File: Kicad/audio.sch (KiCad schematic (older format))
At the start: 70 parts, among them J601 CD Audio In, J602 AC'97 Audio Header, J603 Line Out, U601 TLV320AIC23BPW, U602 STX-4335-5BGP-S1, Y601 12M

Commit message: Fix spaces in MPNs.
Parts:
- FB601, FB602, FB603, FB605, FB606, FB607, FB609, FB610, FB611: MPN BLM21PG221SN1D -> BLM21PG221SN1D
- R606, R607, R611, R612: MPN RMCF0805FT47K5 -> RMCF0805FT47K5
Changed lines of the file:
@@
 F 4 "0" H 4850 1650 50  0001 C CNN "DNP"
 F 5 "RMCF0805FT47K5-ND" H 4850 1650 50  0001 C CNN "Digikey"
-F 6 "RMCF0805FT47K5 " H 4850 1650 50  0001 C CNN "MPN"
+F 6 "RMCF0805FT47K5" H 4850 1650 50  0001 C CNN "MPN"
 F 7 "Stackpole" H 4850 1650 50  0001 C CNN "Manufacturer"
 	1    4850 1650
@@
 F 4 "0" H 5250 1650 50  0001 C CNN "DNP"
 F 5 "RMCF0805FT47K5-ND" H 5250 1650 50  0001 C CNN "Digikey"
-F 6 "RMCF0805FT47K5 " H 5250 1650 50  0001 C CNN "MPN"
+F 6 "RMCF0805FT47K5" H 5250 1650 50  0001 C CNN "MPN"
 F 7 "Stackpole" H 5250 1650 50  0001 C CNN "Manufacturer"
 	1    5250 1650
@@
 F 2 "Inductor_SMD:L_0805_2012Metric_Pad1.15x1.40mm_HandSolder" V 6680 1400 50  0001 C CNN
 F 3 "https://www.murata.com/en-us/products/en-us/products/productdata/8796738977822/ENFA0005.pdf" H 6750 1400 50  0001 C CNN
-F 4 "BLM21PG221SN1D " H 6750 1400 50  0001 C CNN "MPN"
+F 4 "BLM21PG221SN1D" H 6750 1400 50  0001 C CNN "MPN"
 F 5 "0" H 6750 1400 50  0001 C CNN "DNP"
 F 6 "490-1054-1-ND" H 6750 1400 50  0001 C CNN "Digikey"
@@
 F 4 "0" H 4850 2850 50  0001 C CNN "DNP"
 F 5 "RMCF0805FT47K5-ND" H 4850 2850 50  0001 C CNN "Digikey"
-F 6 "RMCF0805FT47K5 " H 4850 2850 50  0001 C CNN "MPN"
+F 6 "RMCF0805FT47K5" H 4850 2850 50  0001 C CNN "MPN"
 F 7 "Stackpole" H 4850 2850 50  0001 C CNN "Manufacturer"
 	1    4850 2850
@@
 F 4 "0" H 5250 2850 50  0001 C CNN "DNP"
 F 5 "RMCF0805FT47K5-ND" H 5250 2850 50  0001 C CNN "Digikey"
-F 6 "RMCF0805FT47K5 " H 5250 2850 50  0001 C CNN "MPN"
+F 6 "RMCF0805FT47K5" H 5250 2850 50  0001 C CNN "MPN"
 F 7 "Stackpole" H 5250 2850 50  0001 C CNN "Manufacturer"
 	1    5250 2850
@@
 F 2 "Inductor_SMD:L_0805_2012Metric_Pad1.15x1.40mm_HandSolder" V 1030 6100 50  0001 C CNN
 F 3 "https://www.murata.com/en-us/products/en-us/products/productdata/8796738977822/ENFA0005.pdf" H 1100 6100 50  0001 C CNN
-F 4 "BLM21PG221SN1D " H 1100 6100 50  0001 C CNN "MPN"
+F 4 "BLM21PG221SN1D" H 1100 6100 50  0001 C CNN "MPN"
 F 5 "0" H 1100 6100 50  0001 C CNN "DNP"
 F 6 "490-1054-1-ND" H 1100 6100 50  0001 C CNN "Digikey"
@@
 F 2 "Inductor_SMD:L_0805_2012Metric_Pad1.15x1.40mm_HandSolder" V 1030 7000 50  0001 C CNN
 F 3 "https://www.murata.com/en-us/products/en-us/products/productdata/8796738977822/ENFA0005.pdf" H 1100 7000 50  0001 C CNN
-F 4 "BLM21PG221SN1D " H 1100 7000 50  0001 C CNN "MPN"
+F 4 "BLM21PG221SN1D" H 1100 7000 50  0001 C CNN "MPN"
 F 5 "0" H 1100 7000 50  0001 C CNN "DNP"
 F 6 "490-1054-1-ND" H 1100 7000 50  0001 C CNN "Digikey"
@@
 F 2 "Inductor_SMD:L_0805_2012Metric_Pad1.15x1.40mm_HandSolder" V 3130 6100 50  0001 C CNN
 F 3 "https://www.murata.com/en-us/products/en-us/products/productdata/8796738977822/ENFA0005.pdf" H 3200 6100 50  0001 C CNN
-F 4 "BLM21PG221SN1D " H 3200 6100 50  0001 C CNN "MPN"
+F 4 "BLM21PG221SN1D" H 3200 6100 50  0001 C CNN "MPN"
 F 5 "0" H 3200 6100 50  0001 C CNN "DNP"
 F 6 "490-1054-1-ND" H 3200 6100 50  0001 C CNN "Digikey"
@@
 F 2 "Inductor_SMD:L_0805_2012Metric_Pad1.15x1.40mm_HandSolder" V 5780 1250 50  0001 C CNN
 F 3 "https://www.murata.com/en-us/products/en-us/products/productdata/8796738977822/ENFA0005.pdf" H 5850 1250 50  0001 C CNN
-F 4 "BLM21PG221SN1D " H 5850 1250 50  0001 C CNN "MPN"
+F 4 "BLM21PG221SN1D" H 5850 1250 50  0001 C CNN "MPN"
 F 5 "0" H 5850 1250 50  0001 C CNN "DNP"
 F 6 "490-1054-1-ND" H 5850 1250 50  0001 C CNN "Digikey"
@@
 F 2 "Inductor_SMD:L_0805_2012Metric_Pad1.15x1.40mm_HandSolder" V 6930 2600 50  0001 C CNN
 F 3 "https://www.murata.com/en-us/products/en-us/products/productdata/8796738977822/ENFA0005.pdf" H 7000 2600 50  0001 C CNN
-F 4 "BLM21PG221SN1D " H 7000 2600 50  0001 C CNN "MPN"
+F 4 "BLM21PG221SN1D" H 7000 2600 50  0001 C CNN "MPN"
 F 5 "0" H 7000 2600 50  0001 C CNN "DNP"
 F 6 "490-1054-1-ND" H 7000 2600 50  0001 C CNN "Digikey"
@@
 F 2 "Inductor_SMD:L_0805_2012Metric_Pad1.15x1.40mm_HandSolder" V 5830 2450 50  0001 C CNN
 F 3 "https://www.murata.com/en-us/products/en-us/products/productdata/8796738977822/ENFA0005.pdf" H 5900 2450 50  0001 C CNN
-F 4 "BLM21PG221SN1D " H 5900 2450 50  0001 C CNN "MPN"
+F 4 "BLM21PG221SN1D" H 5900 2450 50  0001 C CNN "MPN"
 F 5 "0" H 5900 2450 50  0001 C CNN "DNP"
 F 6 "490-1054-1-ND" H 5900 2450 50  0001 C CNN "Digikey"
@@
 F 2 "Inductor_SMD:L_0805_2012Metric_Pad1.15x1.40mm_HandSolder" V 6430 3600 50  0001 C CNN
 F 3 "https://www.murata.com/en-us/products/en-us/products/productdata/8796738977822/ENFA0005.pdf" H 6500 3600 50  0001 C CNN
-F 4 "BLM21PG221SN1D " H 6500 3600 50  0001 C CNN "MPN"
+F 4 "BLM21PG221SN1D" H 6500 3600 50  0001 C CNN "MPN"
 F 5 "0" H 6500 3600 50  0001 C CNN "DNP"
 F 6 "490-1054-1-ND" H 6500 3600 50  0001 C CNN "Digikey"
@@
 F 2 "Inductor_SMD:L_0805_2012Metric_Pad1.15x1.40mm_HandSolder" V 7480 3750 50  0001 C CNN
 F 3 "https://www.murata.com/en-us/products/en-us/products/productdata/8796738977822/ENFA0005.pdf" H 7550 3750 50  0001 C CNN
-F 4 "BLM21PG221SN1D " H 7550 3750 50  0001 C CNN "MPN"
+F 4 "BLM21PG221SN1D" H 7550 3750 50  0001 C CNN "MPN"
 F 5 "0" H 7550 3750 50  0001 C CNN "DNP"
 F 6 "490-1054-1-ND" H 7550 3750 50  0001 C CNN "Digikey"

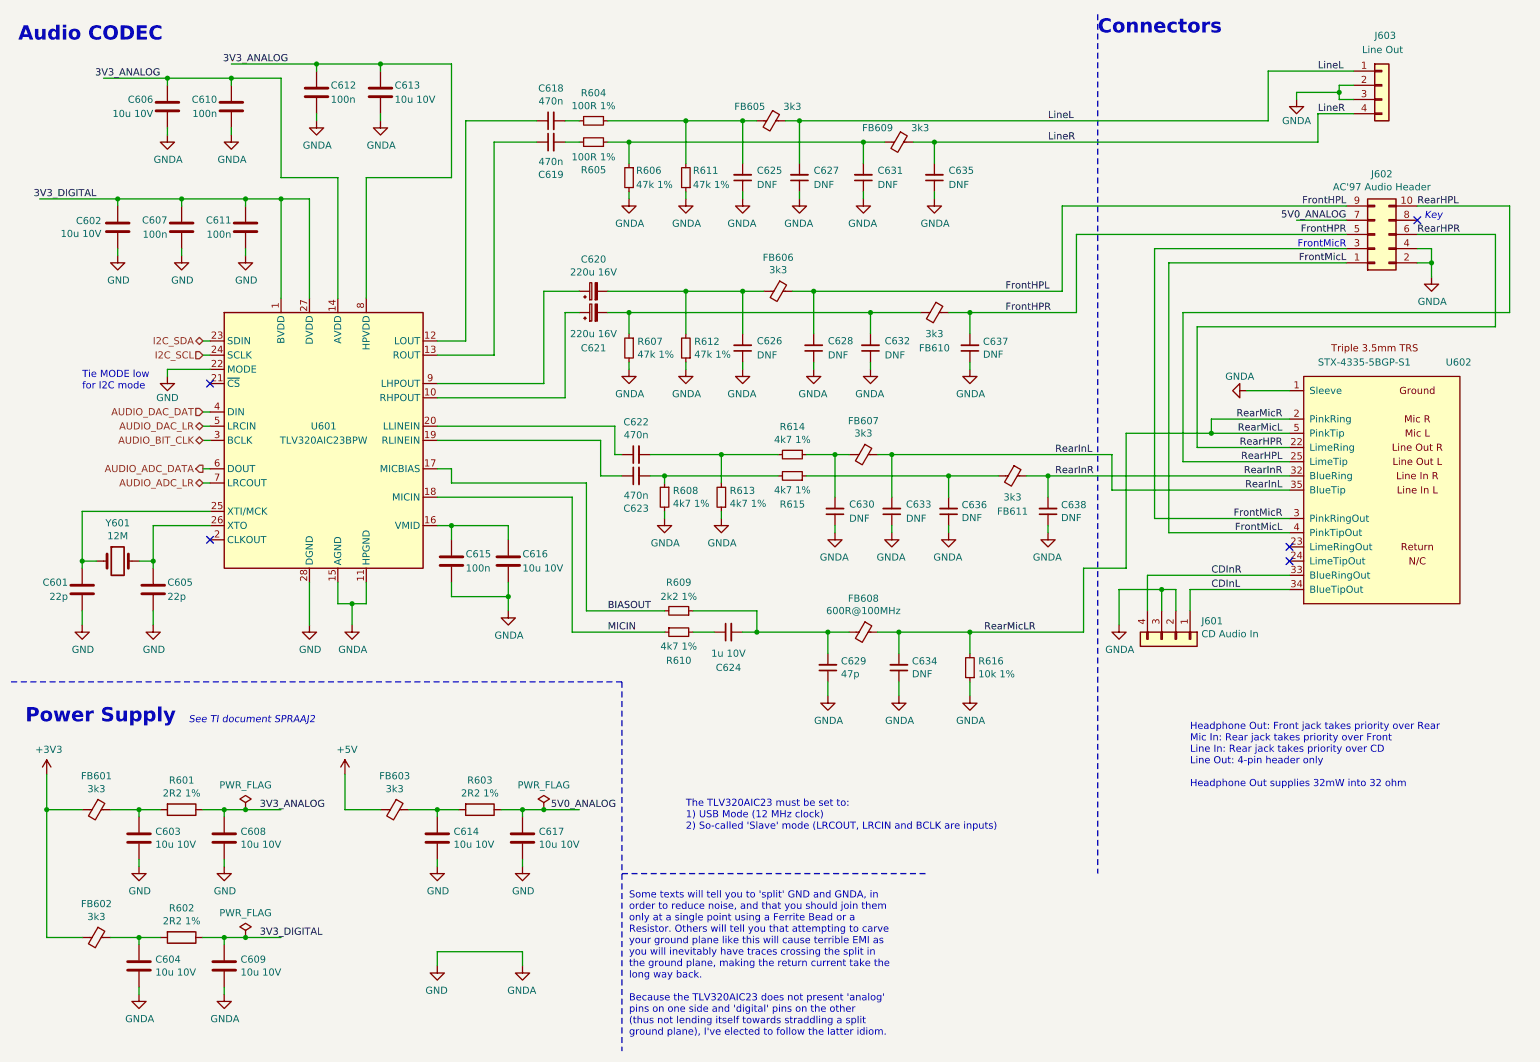
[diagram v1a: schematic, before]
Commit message: Brought in sheets from Neotron Pico.
Also includes DB15HD and PSU 3D models.
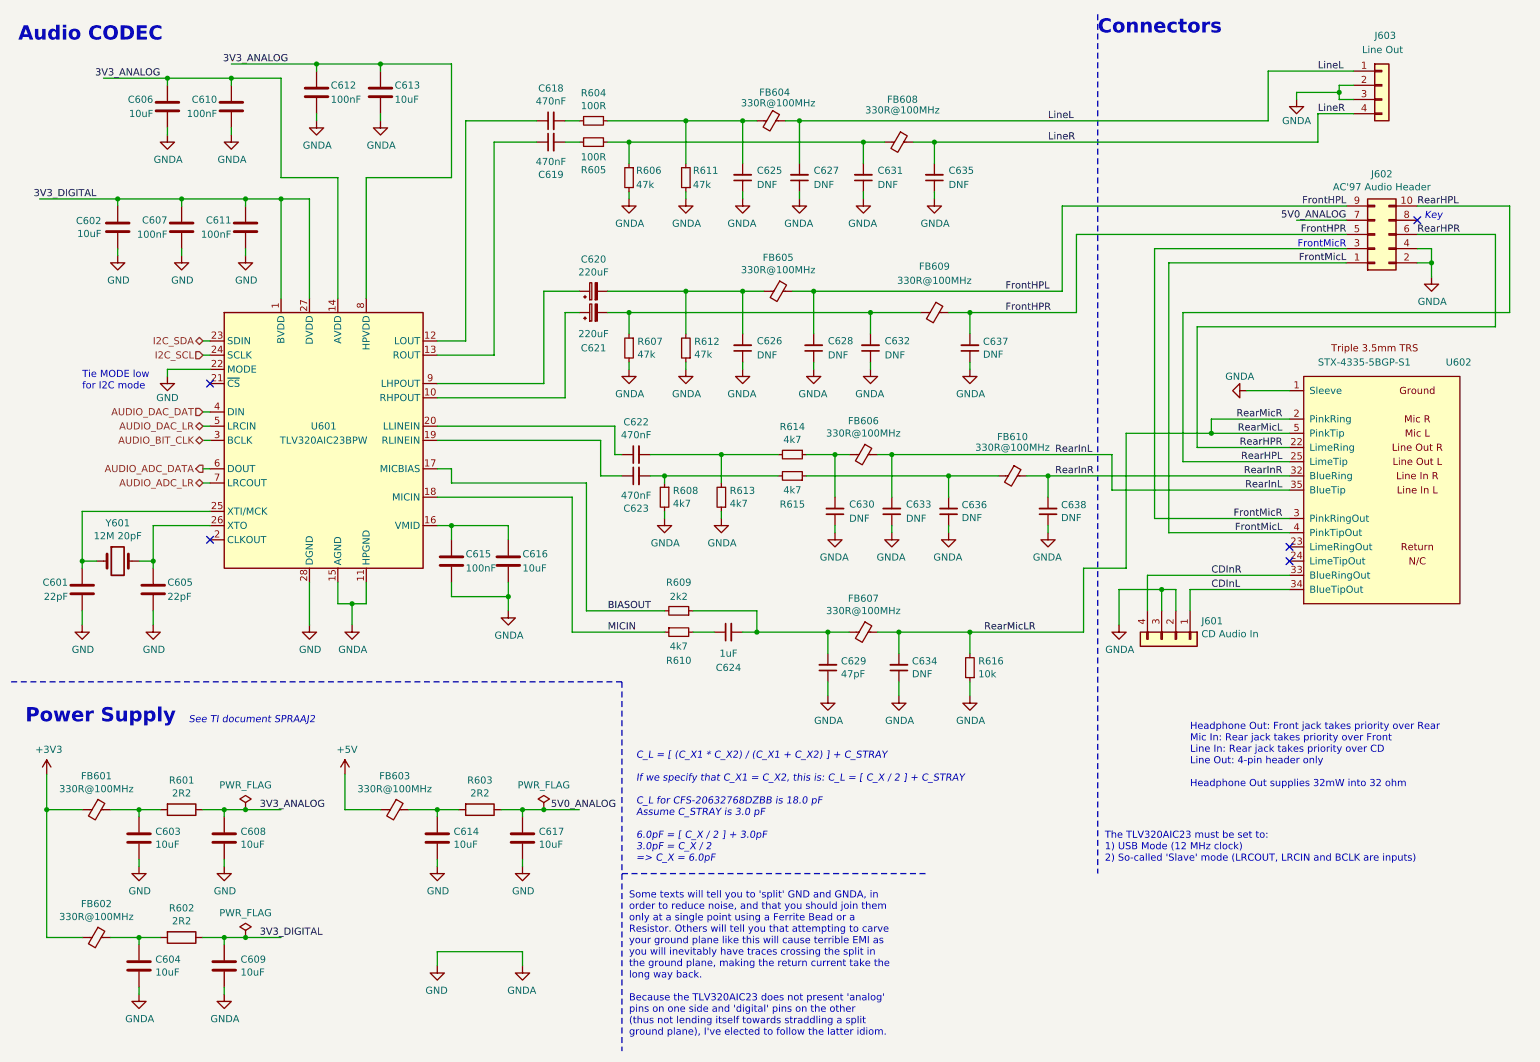
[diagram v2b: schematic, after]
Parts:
- C601, C605: value 22p -> 22pF; LCSC Part# (none) -> C1804; Voltage (none) -> C0G
- C602, C603, C604, C606, C608, C609, C613, C614, C616, C617: value 10u 10V -> 10uF; Digikey 1276-6455-1-ND -> (none); LCSC Part# (none) -> C15850; MPN CL21A106KOQNNNG -> CPL-CAP-X5R-0805-10UF-16V; Manufacturer Samsung -> CPL
- C607, C610, C611, C612, C615: value 100n -> 100nF; Digikey BC1150CT-ND -> (none); LCSC Part# (none) -> C49678; MPN K104K15X7RF5TL2 -> CPL-CAP-X7R-0805-100NF-50V; Manufacturer Vishay -> CPL; Mouser 594-K104K15X7RF5TL2 -> (none)
- C618, C619, C622, C623: value 470n -> 470nF; LCSC Part# (none) -> C13967
- C620, C621: value 220u 16V -> 220uF; footprint Capacitor_THT:CP_Radial_D6.3mm_P2.50mm -> Capacitor_THT:CP_Radial_D8.0mm_P5.00mm; Digikey 493-15424-ND -> (none); MPN UKT1C221MED -> CPL-CAP-ALU-RAD-220UF-50V; Manufacturer Nichicon -> CPL; Mouser 647-UKT1C221MED -> (none)
- C624: value 1u 10V -> 1uF; Digikey 1276-6471-1-ND -> (none); LCSC Part# (none) -> C28323; MPN CL21B105KOFNNNG -> CPL-CAP-X7R-0805-1UF-25V; Manufacturer Samsung -> CPL
- C629: value 47p -> 47pF; LCSC Part# (none) -> C14857
- FB601, FB602, FB603: value 3k3 -> 330R@100MHz; Digikey 490-1054-1-ND -> (none); LCSC Part# (none) -> C1017; MPN BLM21PG221SN1D -> CPL-IND-FER-330OHM-1.5A; Manufacturer Murata -> CPL; Mouser 81-BLM21P221SG -> (none)
- FB604: renamed from FB605; value 3k3 -> 330R@100MHz; Digikey 490-1054-1-ND -> (none); LCSC Part# (none) -> C1017; MPN BLM21PG221SN1D -> CPL-IND-FER-330OHM-1.5A; Manufacturer Murata -> CPL; Mouser 81-BLM21P221SG -> (none)
- FB605: renamed from FB606; value 3k3 -> 330R@100MHz; Digikey 490-1054-1-ND -> (none); LCSC Part# (none) -> C1017; MPN BLM21PG221SN1D -> CPL-IND-FER-330OHM-1.5A; Manufacturer Murata -> CPL; Mouser 81-BLM21P221SG -> (none)
- FB606: renamed from FB607; value 3k3 -> 330R@100MHz; Digikey 490-1054-1-ND -> (none); LCSC Part# (none) -> C1017; MPN BLM21PG221SN1D -> CPL-IND-FER-330OHM-1.5A; Manufacturer Murata -> CPL; Mouser 81-BLM21P221SG -> (none)
- FB607: renamed from FB608; value 600R@100MHz -> 330R@100MHz; Digikey 240-2399-1-ND -> (none); LCSC Part# (none) -> C1017; MPN HZ0805E601R-10 -> CPL-IND-FER-330OHM-1.5A; Manufacturer Laird -> CPL; Mouser 875-HZ0805E601R-10 -> (none)
- FB608: renamed from FB609; value 3k3 -> 330R@100MHz; Digikey 490-1054-1-ND -> (none); LCSC Part# (none) -> C1017; MPN BLM21PG221SN1D -> CPL-IND-FER-330OHM-1.5A; Manufacturer Murata -> CPL; Mouser 81-BLM21P221SG -> (none)
- FB609: renamed from FB610; value 3k3 -> 330R@100MHz; Digikey 490-1054-1-ND -> (none); LCSC Part# (none) -> C1017; MPN BLM21PG221SN1D -> CPL-IND-FER-330OHM-1.5A; Manufacturer Murata -> CPL; Mouser 81-BLM21P221SG -> (none)
- FB610: renamed from FB611; value 3k3 -> 330R@100MHz; Digikey 490-1054-1-ND -> (none); LCSC Part# (none) -> C1017; MPN BLM21PG221SN1D -> CPL-IND-FER-330OHM-1.5A; Manufacturer Murata -> CPL; Mouser 81-BLM21P221SG -> (none)
- R601, R602, R603: value 2R2 1% -> 2R2; LCSC Part# (none) -> C17521
- R604, R605: value 100R 1% -> 100R; Digikey RMCF0805FT100R-ND -> (none); LCSC Part# (none) -> C17408; MPN RMCF0805FT100R -> CPL-RES-0805-100-0.125W; Manufacturer Stackpole -> CPL
- R606, R607, R611, R612: value 47k 1% -> 47k; LCSC Part# (none) -> C17713
- R608, R610, R613, R614, R615: value 4k7 1% -> 4k7; Digikey RMCF0805FT4K75-ND -> (none); LCSC Part# (none) -> C17673; MPN RMCF0805FT4K75 -> CPL-RES-0805-4.7K-0.125W; Manufacturer Stackpole -> CPL
- R609: value 2k2 1% -> 2k2; LCSC Part# (none) -> C17520
- R616: value 10k 1% -> 10k; Digikey RMCF0805FT10K0-ND -> (none); LCSC Part# (none) -> C17414; MPN RMCF0805FT10K0 -> CPL-RES-0805-10K-0.125W; Manufacturer Stackpole -> CPL
- U601: LCSC Part# (none) -> C9915
- Y601: value 12M -> 12M 20pF; footprint Crystal:Crystal_HC49-4H_Vertical -> Crystal:Crystal_SMD_5032-2Pin_5.0x3.2mm_HandSoldering; Digikey 535-9037-ND -> (none); LCSC Part# (none) -> C90883; MPN ABL-12.000MHZ-B2 -> CPL-OSC-CRY-12MHZ-18PF; Manufacturer Abracon -> CPL; Mouser 815-ABL-12-B2 -> (none)
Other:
- note added: "C_L = [ (C_X1 * C_X2) / (C_X1 + C_X2) ] + C_STRAY\n\nIf we specify that C_X1 = C_X2, this is: C_L = [ C_X / 2 ] + C_STRAY\n\nC_L for CFS-20632768DZBB is 18.0 pF\nAssume C_STRAY is 3.0 pF \n\n6.0pF = [ C_X / 2 ] + 3.0pF\n3.0pF = C_X / 2\n=> C_X = 6.0pF"

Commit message: Merge in more changes.
Mostly lowering voltage tolerances to minimum required.
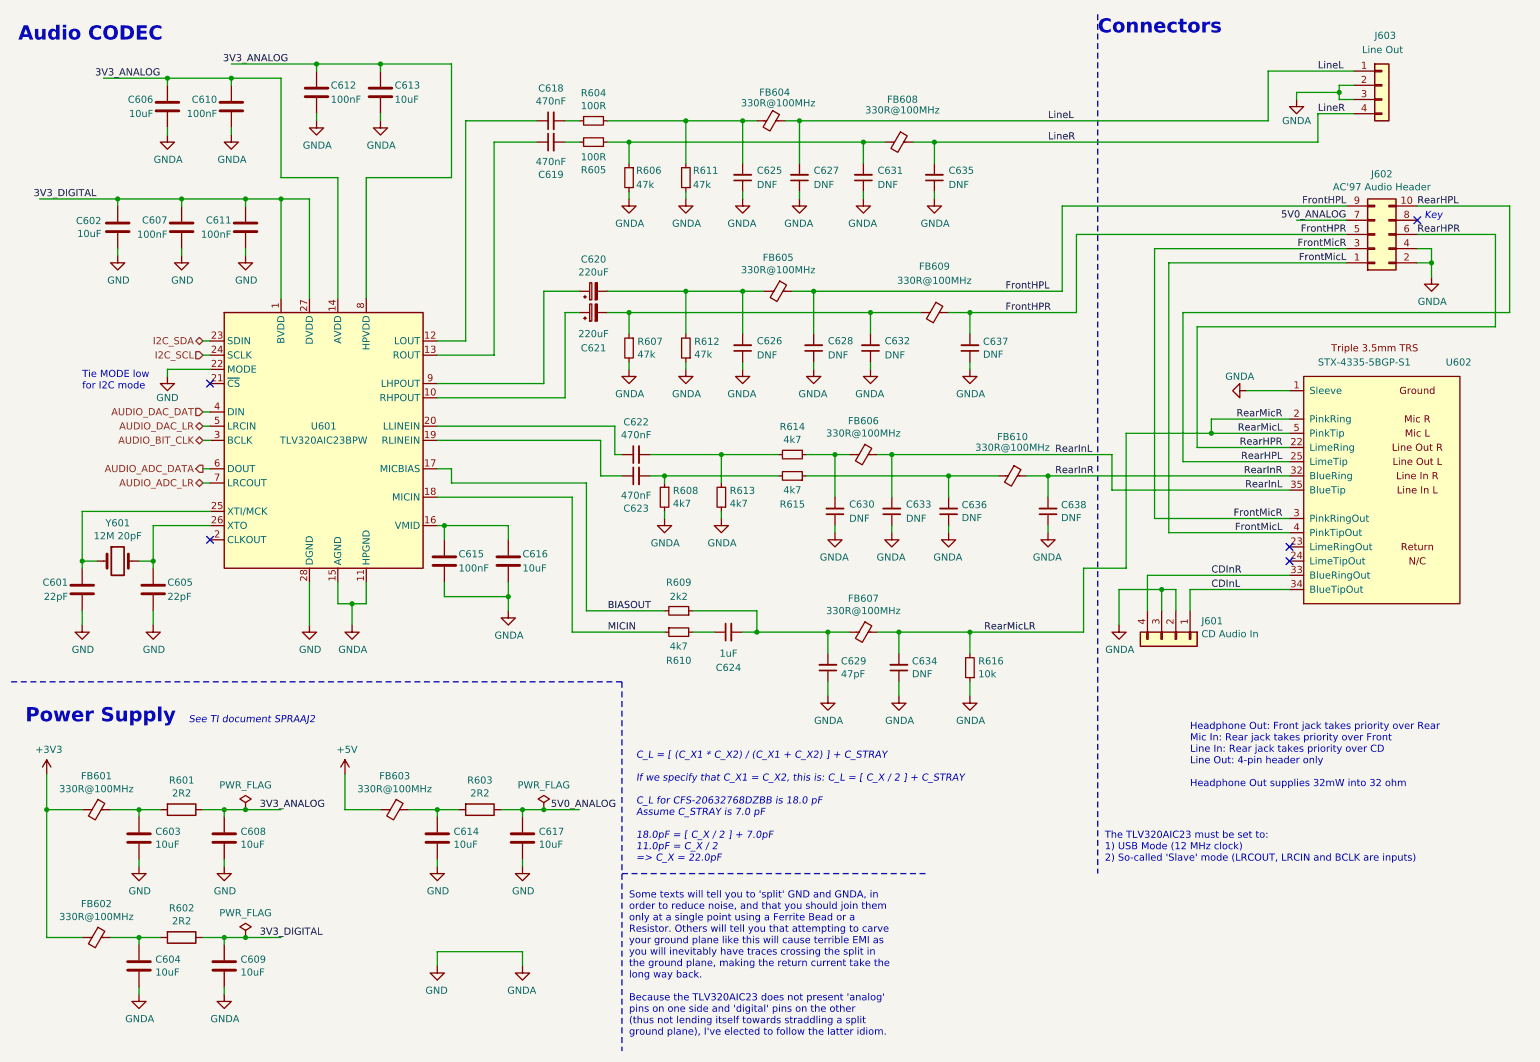
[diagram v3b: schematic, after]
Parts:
- C601, C605: Tolerance (none) -> C0G; Voltage C0G -> 16V
- C602, C603, C604, C606, C607, C608, C609, C610, C611, C612, C613, C615, C616: Tolerance (none) -> X5R; Voltage (none) -> 10V
- C614, C617: Tolerance (none) -> X5R; Voltage (none) -> 16V
- C618, C619, C622, C623: MPN FG18X7R1H474KRT06 -> CL21B474KBFNNNE; Tolerance (none) -> X5R; Voltage (none) -> 6.3V
- C620, C621: Tolerance (none) -> 20%; Voltage (none) -> 6.3V
- C624: Tolerance (none) -> X5R; Voltage (none) -> 6.3V
- C629: Tolerance (none) -> C0G; Voltage (none) -> 6.3V
- FB601, FB602, FB603, FB604, FB605, FB606, FB607, FB608, FB609, FB610: Tolerance (none) -> 1.5A
- R601, R602, R603, R604, R605, R606, R607, R608, R609, R610, R611, R612, R613, R614, R615, R616: Tolerance (none) -> 1%
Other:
- note added: "C_L = [ (C_X1 * C_X2) / (C_X1 + C_X2) ] + C_STRAY\n\nIf we specify that C_X1 = C_X2, this is: C_L = [ C_X / 2 ] + C_STRAY\n\nC_L for CFS-20632768DZBB is 18.0 pF\nAssume C_STRAY is 7.0 pF \n\n18.0pF = [ C_X / 2 ] + 7.0pF\n11.0pF = C_X / 2\n=> C_X = 22.0pF"
- note removed: "C_L = [ (C_X1 * C_X2) / (C_X1 + C_X2) ] + C_STRAY\n\nIf we specify that C_X1 = C_X2, this is: C_L = [ C_X / 2 ] + C_STRAY\n\nC_L for CFS-20632768DZBB is 18.0 pF\nAssume C_STRAY is 3.0 pF \n\n6.0pF = [ C_X / 2 ] + 3.0pF\n3.0pF = C_X / 2\n=> C_X = 6.0pF"
- note removed: "FrontMicR"
- moved on the sheet: C615
